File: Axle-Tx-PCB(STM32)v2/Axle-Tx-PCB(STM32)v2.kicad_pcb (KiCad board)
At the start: 2 copper layers, 14 parts, among them J1 SWD Con, J2 nRF24L01 Con

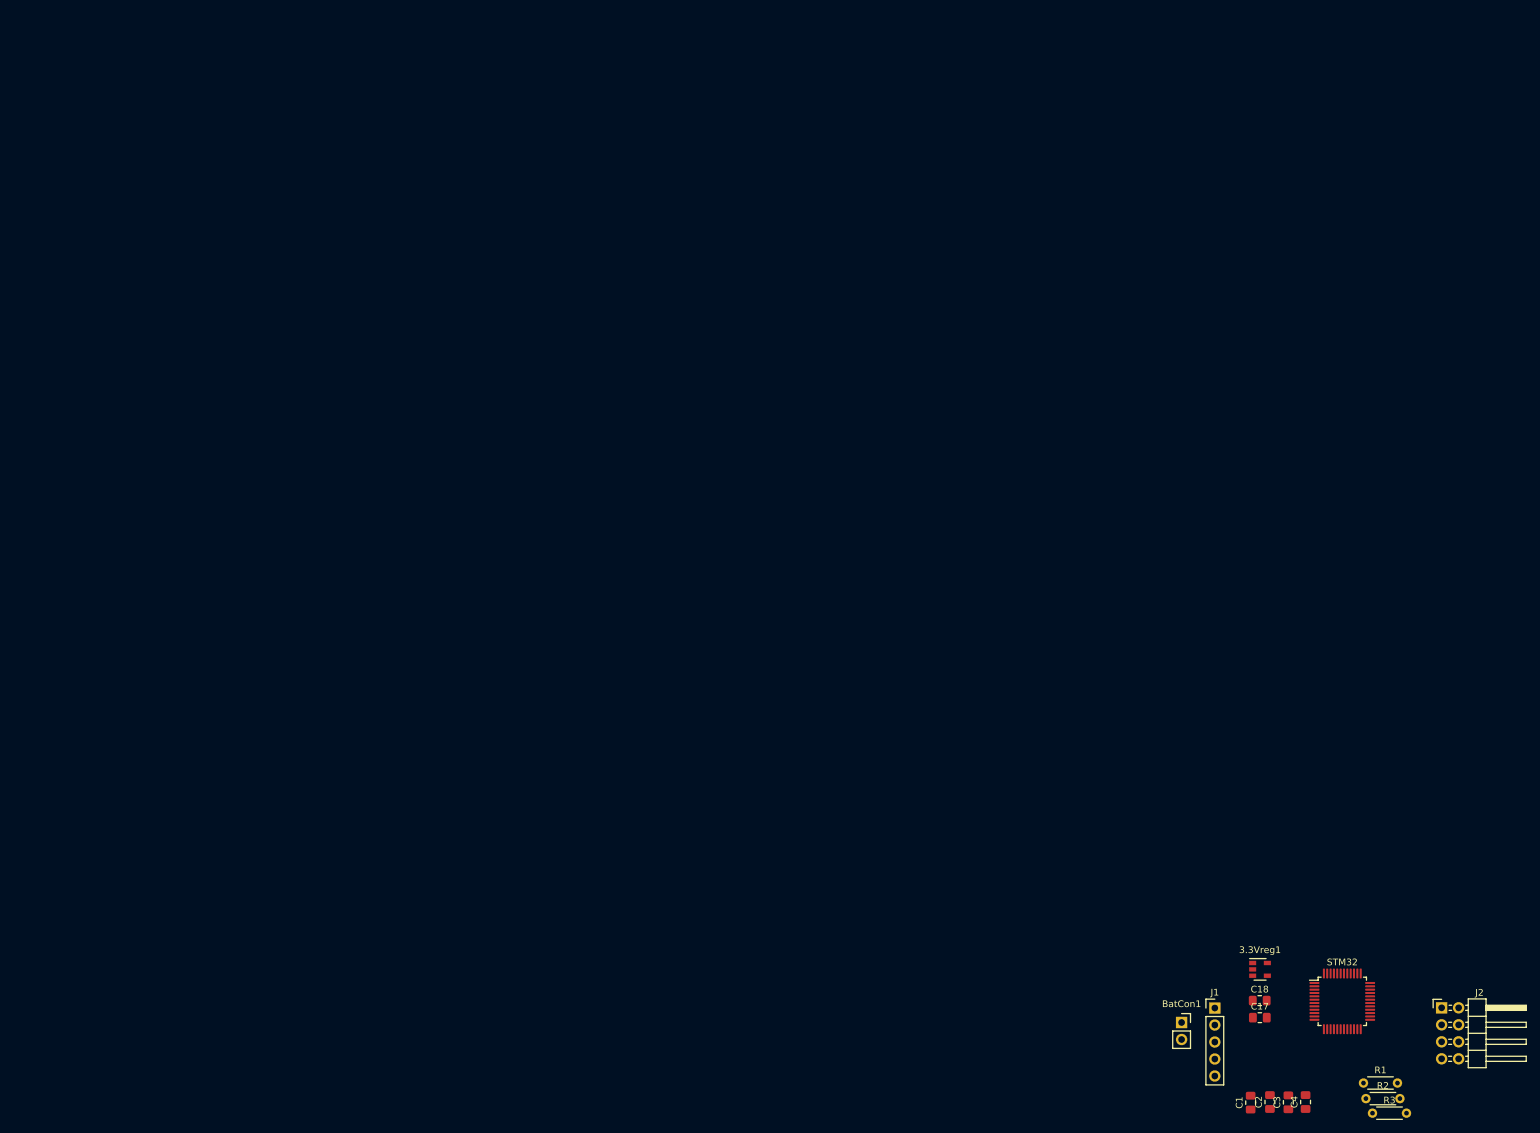
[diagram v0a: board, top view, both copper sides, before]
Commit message: axle-side PCB complete, programming/breakout board complete, midway through recieving-end PCB. parts list has been finalized, ready to order when PCB files have been sent off for manufacturing
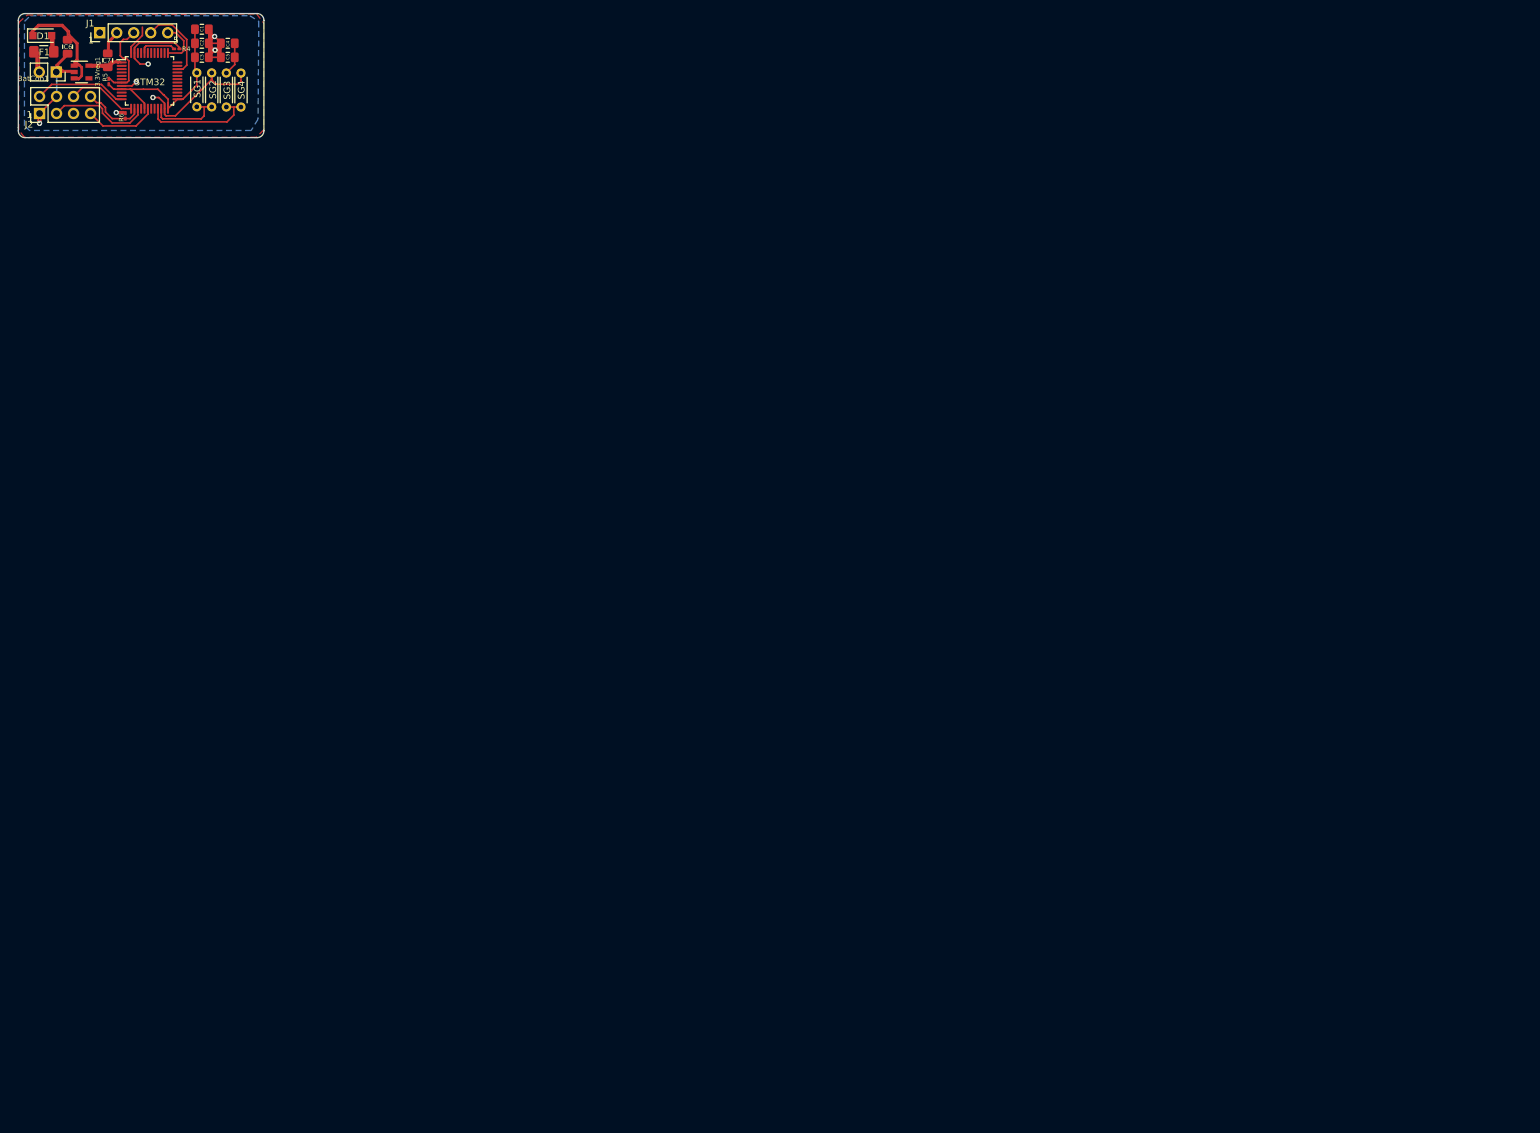
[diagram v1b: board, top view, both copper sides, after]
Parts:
- added C5: 10nF, Capacitor_SMD:C_0805_2012Metric_Pad1.18x1.45mm_HandSolder, F.Cu at (34.0, -14.7)
- added D1: D, Diode_SMD:D_SOD-123F, F.Cu at (6.32, -18.0)
- added F1: Fuse(160mA), Fuse:Fuse_1206_3216Metric_Pad1.42x1.75mm_HandSolder, F.Cu at (6.55, -15.6)
- added R4: 10k, Resistor_SMD:R_0201_0603Metric_Pad0.64x0.40mm_HandSolder, F.Cu at (26.4, -16.0)
- added R5: 10k, Resistor_SMD:R_0201_0603Metric_Pad0.64x0.40mm_HandSolder, F.Cu at (16.3, -11.1)
- added R6: 10k, Resistor_SMD:R_0201_0603Metric_Pad0.64x0.40mm_HandSolder, F.Cu at (18.7, -5.99)
- added SG4: gauge, Resistor_THT:R_Axial_DIN0204_L3.6mm_D1.6mm_P5.08mm_Horizontal, F.Cu at (36.0, -7.32)
- C1: value C -> 4.7uF
- C2, C3, C4: value C -> 10nF
- C6: renamed from C17; value C -> 1uF
- C7: renamed from C18; value C -> 1uF
- J2: footprint Connector_PinHeader_2.54mm:PinHeader_2x04_P2.54mm_Horizontal -> Connector_PinHeader_2.54mm:PinHeader_2x04_P2.54mm_Vertical
- SG1: renamed from R1; value R -> gauge
- SG2: renamed from R3; value R -> gauge
- SG3: renamed from R2; value R -> gauge
- moved J2 248.5 mm to (5.92, -6.35), turned to 90 degrees
- moved SG1 230.6 mm to (29.4, -12.4), turned to 270 degrees
- moved C6 229.8 mm to (10.1, -16.3), turned to 270 degrees
- moved SG2 229.6 mm to (31.6, -7.34), turned to 90 degrees
- moved SG3 229.1 mm to (33.8, -12.4), turned to 270 degrees
- moved C4 225.8 mm to (34.0, -16.8), turned to 180 degrees
- moved C3 225.3 mm to (30.2, -14.7), turned to 0 degrees
- moved STM32 225.1 mm to (22.4, -11.2)
- moved C2 224.7 mm to (30.2, -16.8), turned to 0 degrees
- moved C1 224.3 mm to (30.2, -18.9), turned to 0 degrees
- moved C7 222.2 mm to (16.1, -14.3), turned to 90 degrees
- moved J1 221.4 mm to (14.9, -18.4), turned to 90 degrees
- moved 3.3Vreg1 221.4 mm to (12.2, -12.5)
- moved BatCon1 220.1 mm to (8.41, -12.5), turned to 270 degrees
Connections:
- 3.3Vreg1 pad 2: GND -> SPI1-MISO
- 3.3Vreg1 pad 5: +3V3 -> VBAT
- BatCon1 pad 1: GND -> SPI1-MISO
- C1 pad 2: GND -> SPI1-MISO
- C2 pad 2: GND -> SPI1-MISO
- C3 pad 2: GND -> SPI1-MISO
- C4 pad 2: GND -> SPI1-MISO
- C6 pad 2: GND -> SPI1-MISO
- C7 pad 1: +3V3 -> VBAT
- C7 pad 2: GND -> SPI1-MISO
- J1 pad 2: GND -> SPI1-MISO
- J2 pad 1: GND -> SPI1-MISO
- J2 pad 2: CE -> SPI1-CE
- J2 pad 3: SCK -> SPI1-SCK
- J2 pad 4: MISO -> SPI1-MISO
- J2 pad 6: CSn -> SPI1-CSn
- J2 pad 7: MOSI -> SPI1-MOSI
- J2 pad 8: IRO -> SPI1-IRQ
- SG1 pad 2: ADC- -> SDADC-AIN8m
- SG2 pad 1: ADC- -> SDADC-AIN8m
- SG2 pad 2: GND -> SPI1-MISO
- SG3 pad 2: ADC+ -> SDADC1-AIN8p
- STM32 pad 1: Net-(STM32-Pad1) -> VBAT
- STM32 pad 12: Net-(STM32-Pad12) -> SPI1-CE
- STM32 pad 13: Net-(STM32-Pad13) -> SPI1-CSn
- STM32 pad 14: Net-(STM32-Pad14) -> SPI1-IRQ
- STM32 pad 15: Net-(STM32-Pad15) -> SPI1-SCK
- STM32 pad 18: Net-(STM32-Pad18) -> SPI1-MOSI
- STM32 pad 21: Net-(STM32-Pad21) -> SDADC1-AIN8p
- STM32 pad 22: Net-(STM32-Pad22) -> SDADC-AIN8m
- STM32 pad 23: Net-(STM32-Pad23) -> SPI1-MISO
- STM32 pad 24: Net-(STM32-Pad24) -> +3V3
- STM32 pad 25: Net-(STM32-Pad25) -> +3V3
- STM32 pad 47: GND -> SPI1-MISO
- STM32 pad 8: Net-(STM32-Pad8) -> SPI1-MISO
- STM32 pad 9: Net-(STM32-Pad9) -> +3V3
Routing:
- net SPI1-MISO: track 0.00 -> 98.9 mm, vias 0 -> 7
- net +3V3: track 0.00 -> 39.0 mm
- net Net-(3.3Vreg1-Pad1): track 0.00 -> 34.6 mm
- net SDADC1-AIN8p: track 0.00 -> 16.8 mm
- net SPI1-SCK: track 0.00 -> 15.5 mm
- net SPI1-CE: track 0.00 -> 13.9 mm
- net VBAT: track 0.00 -> 13.6 mm
- net NRST: track 0.00 -> 12.5 mm
- net PA13-SWDIO: track 0.00 -> 12.3 mm
- net SDADC-AIN8m: track 0.00 -> 11.5 mm
- net SPI1-MOSI: track 0.00 -> 10.9 mm
- net SPI1-CSn: track 0.00 -> 10.5 mm
- net SPI1-IRQ: track 0.00 -> 9.40 mm
- net Net-(BatCon1-Pad2): track 0.00 -> 9.35 mm
- net PA14-SWCLK: track 0.00 -> 6.93 mm
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- added copper zone on F.Cu, net +3V3
- added copper zone on B.Cu, net SPI1-MISO
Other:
- board outline added: 36.7 x 18.5 mm
- board text added: "1"
- board text added: "5"

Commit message: final versions of PCBs, ordered through JLCPCB 2020-12-30
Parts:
- removed C5: 10nF, Capacitor_SMD:C_0805_2012Metric_Pad1.18x1.45mm_HandSolder
- moved C2 65.8 mm to (62.4, 40.5), turned to 270 degrees
- moved C1 64.5 mm to (55.4, 40.4), turned to 270 degrees
- moved R5 63.4 mm to (42.2, 46.8)
- moved 3.3Vreg1 63.2 mm to (37.8, 45.2)
- moved BatCon1 63.2 mm to (34.0, 45.2)
- moved D1 63.2 mm to (31.9, 39.8)
- moved STM32 63.2 mm to (48.0, 46.5)
- moved C6 63.2 mm to (35.7, 41.4)
- moved C7 63.2 mm to (41.7, 43.5)
- moved F1 63.2 mm to (32.2, 42.2)
- moved J1 63.2 mm to (40.5, 39.3)
- moved J2 63.2 mm to (31.5, 51.4)
- moved R6 63.2 mm to (44.3, 51.8)
- moved SG1 63.2 mm to (55.0, 45.3)
- moved SG2 63.2 mm to (57.2, 50.4)
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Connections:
- 3.3Vreg1 pad 2: SPI1-MISO -> GND
- 3.3Vreg1 pad 5: VBAT -> +3V3
- BatCon1 pad 1: SPI1-MISO -> GND
- C1 pad 2: SPI1-MISO -> GND
- C2 pad 2: SPI1-MISO -> GND
- C3 pad 2: SPI1-MISO -> GND
- C4 pad 2: SPI1-MISO -> GND
- C6 pad 2: SPI1-MISO -> GND
- C7 pad 1: VBAT -> +3V3
- C7 pad 2: SPI1-MISO -> GND
- J1 pad 2: SPI1-MISO -> GND
- J2 pad 1: SPI1-MISO -> GND
- R4 pad 2: SPI1-MISO -> GND
- R6 pad 1: SPI1-MISO -> GND
- SG2 pad 2: SPI1-MISO -> GND
- SG4 pad 2: SPI1-MISO -> GND
- STM32 pad 1: VBAT -> +3V3
- STM32 pad 16: Net-(STM32-Pad16) -> SPI1-MISO
- STM32 pad 23: SPI1-MISO -> GND
- STM32 pad 47: SPI1-MISO -> GND
- STM32 pad 8: SPI1-MISO -> GND
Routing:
- net SPI1-MISO: track 98.9 -> 23.1 mm, vias 7 -> 1
- net GND: track 0.00 -> 48.4 mm, vias 0 -> 10
- net VBAT: track 13.6 -> 0.00 mm
- net +3V3: track 39.0 -> 29.7 mm
- net NRST: track 12.5 -> 10.8 mm, vias 0 -> 1
- net PA13-SWDIO: track 12.3 -> 13.9 mm
- net PA14-SWCLK: track 6.93 -> 7.84 mm
- net SDADC-AIN8m: track 11.5 -> 12.2 mm
- net SPI1-MOSI: track 10.9 -> 11.1 mm, vias 0 -> 1
- added copper zone on B.Cu, net GND
- removed copper zone on B.Cu, net SPI1-MISO

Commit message: PCB's ready for final review before order
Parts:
- removed 3.3Vreg1: LD39015M33R, Package_TO_SOT_SMD:SOT-23-5
- removed BatCon1: 4P2C, Connector_PinSocket_2.54mm:PinSocket_1x02_P2.54mm_Vertical
- removed J2: nRF24L01 Con, Connector_PinHeader_2.54mm:PinHeader_2x04_P2.54mm_Vertical
- added 3v3reg1: LD39015M33R, Package_TO_SOT_SMD:SOT-23-5, F.Cu at (61.1, 45.0)
- added B+1: 4P2C, Connector_PinSocket_2.54mm:PinSocket_1x02_P2.54mm_Vertical, F.Cu at (63.9, 49.9)
- added LED1: LED, LED_SMD:LED_1206_3216Metric_Pad1.42x1.75mm_HandSolder, F.Cu at (61.0, 41.0)
- added LED2: LED, LED_SMD:LED_1206_3216Metric_Pad1.42x1.75mm_HandSolder, F.Cu at (61.0, 38.8)
- added R1: 2k2, Resistor_SMD:R_0603_1608Metric_Pad1.05x0.95mm_HandSolder, F.Cu at (56.1, 40.4)
- added R2: 2k2, Resistor_SMD:R_0603_1608Metric_Pad1.05x0.95mm_HandSolder, F.Cu at (56.1, 38.6)
- added SWD1: SWDConnector, Connector_PinHeader_2.54mm:PinHeader_1x04_P2.54mm_Vertical, F.Cu at (59.4, 50.0)
- J1: value SWD Con -> nRF24; footprint Connector_PinHeader_2.54mm:PinHeader_1x05_P2.54mm_Vertical -> Connector_PinHeader_2.54mm:PinHeader_2x04_P2.54mm_Vertical
- R4, R5, R6: footprint Resistor_SMD:R_0201_0603Metric_Pad0.64x0.40mm_HandSolder -> Resistor_SMD:R_0603_1608Metric_Pad1.05x0.95mm_HandSolder
- moved SG3 35.6 mm to (24.3, 39.8), turned to 0 degrees
- moved D1 34.4 mm to (66.1, 43.9)
- moved F1 34.0 mm to (65.8, 46.6), turned to 0 degrees
- moved SG4 33.4 mm to (29.4, 41.9), turned to 180 degrees
- moved C6 31.1 mm to (66.8, 40.5), turned to 90 degrees
- moved SG1 30.8 mm to (24.3, 46.2), turned to 0 degrees
- moved SG2 28.6 mm to (29.4, 44.1), turned to 180 degrees
- moved C4 21.5 mm to (39.7, 47.2), turned to 90 degrees
- moved C3 19.5 mm to (41.2, 50.6), turned to 180 degrees
- moved C2 17.9 mm to (44.7, 38.4), turned to 0 degrees
- moved R6 16.5 mm to (28.2, 48.5), turned to 0 degrees
- moved C7 16.4 mm to (58.0, 44.9)
- moved R5 13.1 mm to (52.0, 38.1), turned to 180 degrees
- moved J1 8.26 mm to (32.3, 39.0), turned to 0 degrees
- moved R4 5.09 mm to (53.6, 46.6)
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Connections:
- J1 pad 1: +3V3 -> GND
- J1 pad 2: GND -> +3V3
- J1 pad 3: NRST -> SPI1-CE
- J1 pad 4: PA13-SWDIO -> SPI1-CSn
- J1 pad 5: PA14-SWCLK -> SPI1-SCK
- R5 pad 2: NRST -> Net-(R5-Pad2)
- STM32 pad 7: NRST -> Net-(R5-Pad2)
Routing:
- net Net-(3v3reg1-Pad1): track 34.6 -> 9.24 mm
- net GND: track 48.4 -> 25.4 mm
- net SDADC1-AIN8p: track 16.8 -> 31.5 mm, vias 0 -> 1
- net NRST: track 10.8 -> 0.00 mm, vias 1 -> 0
- net SPI1-IRQ: track 9.40 -> 20.0 mm, vias 0 -> 1
- net SDADC-AIN8m: track 12.2 -> 22.0 mm, vias 0 -> 1
- net PA13-SWDIO: track 13.9 -> 5.07 mm
- net Net-(R2-Pad1): track 0.00 -> 8.73 mm
- net Net-(R1-Pad1): track 0.00 -> 7.97 mm
- net Net-(R5-Pad2): track 0.00 -> 6.77 mm
- net SPI1-MISO: track 23.1 -> 16.7 mm
- net Net-(B+1-Pad2): track 9.35 -> 3.79 mm
- net SPI1-SCK: track 15.5 -> 10.5 mm
- net SPI1-MOSI: track 11.1 -> 7.52 mm, vias 1 -> 0
- net Net-(LED2-Pad2): track 0.00 -> 3.46 mm
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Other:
- board size 36.7 x 18.5 mm -> 45.8 x 15.7 mm
- board text added: "."
- board text removed: "1"
- board text removed: "5"
